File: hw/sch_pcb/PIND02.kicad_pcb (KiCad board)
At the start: 2 copper layers, 40.1 x 40.1 mm, 8 parts, among them J1 Umin ... Umax, M1 HOLE M3, M2 HOLE M3, M3 HOLE, M4 HOLE

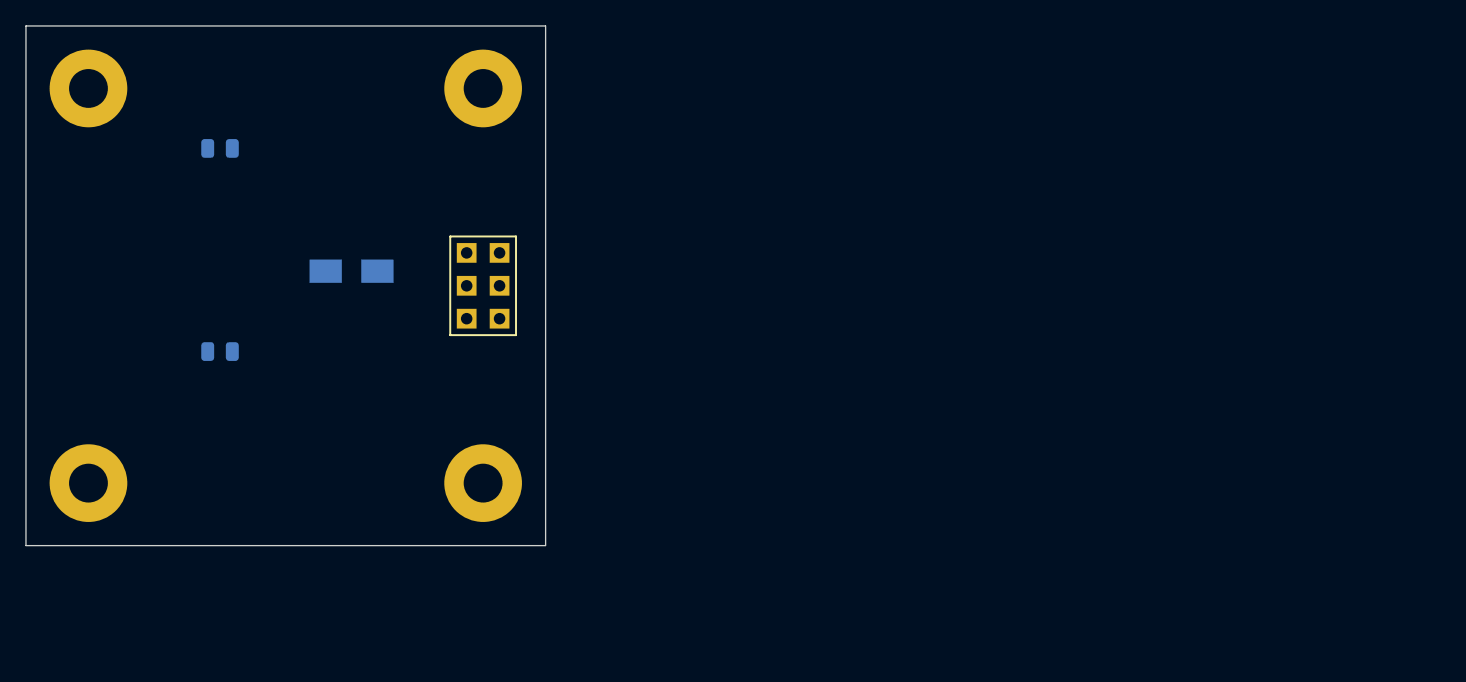
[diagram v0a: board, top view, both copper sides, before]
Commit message: Assing footprints to components. Starting of PCB design.
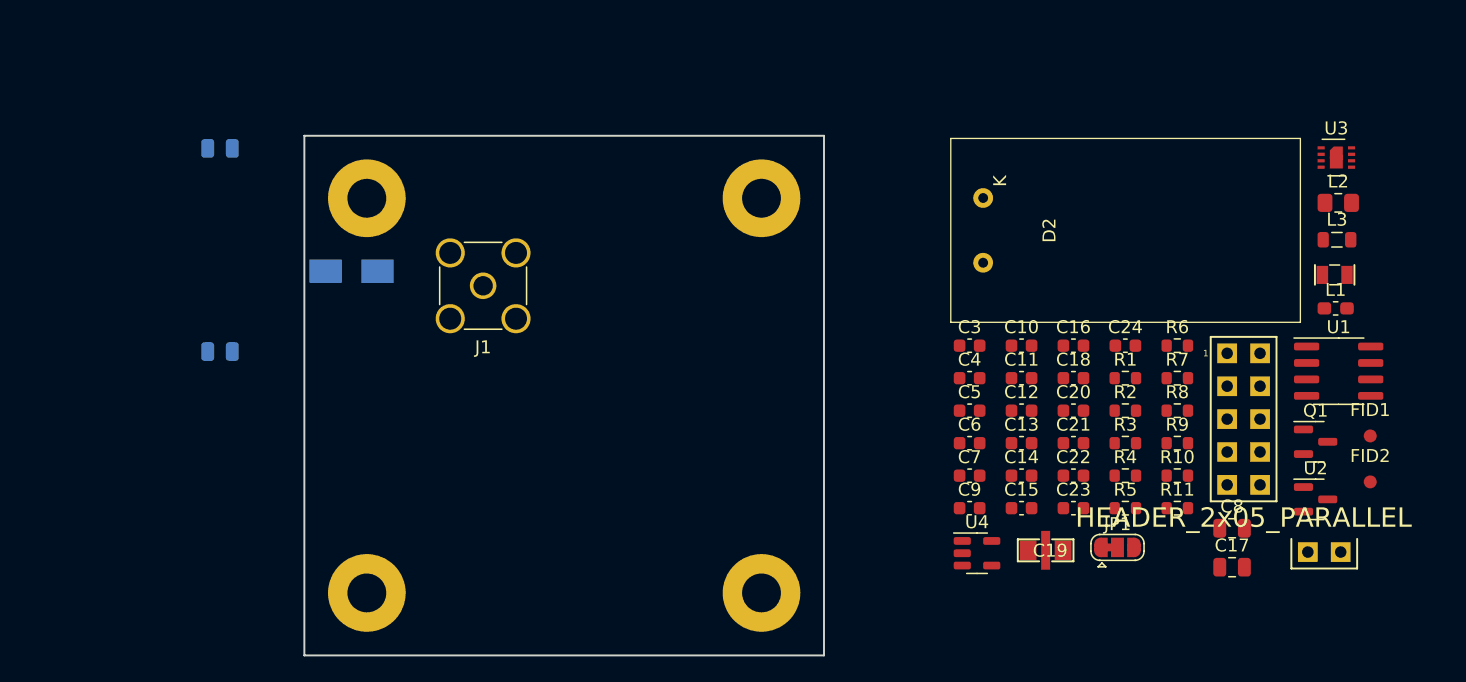
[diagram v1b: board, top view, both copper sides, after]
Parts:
- added C10: 10uF, Capacitor_SMD:C_0603_1608Metric, F.Cu at (183.8, 101.1)
- added C11: 100nF, Capacitor_SMD:C_0603_1608Metric, F.Cu at (183.8, 103.7)
- added C12: 1uF, Capacitor_SMD:C_0603_1608Metric, F.Cu at (183.8, 106.2)
- added C13: 100nF, Capacitor_SMD:C_0603_1608Metric, F.Cu at (183.8, 108.7)
- added C14: 100nF, Capacitor_SMD:C_0603_1608Metric, F.Cu at (183.8, 111.2)
- added C15: 1uF, Capacitor_SMD:C_0603_1608Metric, F.Cu at (183.8, 113.7)
- added C16: 3n3, Capacitor_SMD:C_0603_1608Metric, F.Cu at (187.8, 101.1)
- added C17: 100nF, Capacitor_SMD:C_0805_2012Metric, F.Cu at (200.1, 118.3)
- added C18: 100nF, Capacitor_SMD:C_0603_1608Metric, F.Cu at (187.8, 103.7)
- added C19: NFM21PC105-1uF, Mlab_L:FIR_0805, F.Cu at (185.7, 117.0)
- added C20: 100nF, Capacitor_SMD:C_0603_1608Metric, F.Cu at (187.8, 106.2)
- added C21: 10uF, Capacitor_SMD:C_0603_1608Metric, F.Cu at (187.8, 108.7)
- added C22: 100nF, Capacitor_SMD:C_0603_1608Metric, F.Cu at (187.8, 111.2)
- added C23: 10uF, Capacitor_SMD:C_0603_1608Metric, F.Cu at (187.8, 113.7)
- added C24: 10uF, Capacitor_SMD:C_0603_1608Metric, F.Cu at (191.8, 101.1)
- added C3: 100nF, Capacitor_SMD:C_0603_1608Metric, F.Cu at (179.8, 101.1)
- added C4: 10uF, Capacitor_SMD:C_0603_1608Metric, F.Cu at (179.8, 103.7)
- added C5: 1uF, Capacitor_SMD:C_0603_1608Metric, F.Cu at (179.8, 106.2)
- added C6: 100nF, Capacitor_SMD:C_0603_1608Metric, F.Cu at (179.8, 108.7)
- added C7: 10uF, Capacitor_SMD:C_0603_1608Metric, F.Cu at (179.8, 111.2)
- added C8: 1pF/NP0 251R15S1R0AV4E, Capacitor_SMD:C_0805_2012Metric, F.Cu at (200.1, 115.2)
- added C9: 10uF, Capacitor_SMD:C_0603_1608Metric, F.Cu at (179.8, 113.7)
- added D2: S2744-09, Mlab_D:HAMAMATSU_S2744-09, F.Cu at (191.9, 92.2)
- added FID1: Fiducial, Fiducial:Fiducial_1mm_Mask2mm, F.Cu at (210.8, 108.1)
- added FID2: Fiducial, Fiducial:Fiducial_1mm_Mask2mm, F.Cu at (210.8, 111.7)
- added J2: HEADER_2x05_PARALLEL, Mlab_Pin_Headers:Straight_2x05, F.Cu at (201.0, 106.8)
- added J3: HEADER_2x01, Mlab_Pin_Headers:Straight_2x01, F.Cu at (207.2, 117.1)
- added JP1: Address select, Jumper:SolderJumper-3_P1.3mm_Bridged12_RoundedPad1.0x1.5mm, F.Cu at (191.2, 116.7)
- added L1: NL03KT330, Inductor_SMD:L_0603_1608Metric_Pad1.05x0.95mm_HandSolder, F.Cu at (208.1, 98.3)
- added L2: DFE252012P-4R7M, Inductor_SMD:L_0805_2012Metric_Pad1.15x1.40mm_HandSolder, F.Cu at (208.3, 90.1)
- added L3: L, Inductor_SMD:L_0805_2012Metric, F.Cu at (208.2, 93.0)
- added Q1: 2SK2394-6, Package_TO_SOT_SMD:SOT-23, F.Cu at (206.5, 108.6)
- added R1: 470R, Resistor_SMD:R_0603_1608Metric, F.Cu at (191.8, 103.7)
- added R10: 4k7, Resistor_SMD:R_0603_1608Metric, F.Cu at (195.9, 111.2)
- added R11: 1k, Resistor_SMD:R_0603_1608Metric, F.Cu at (195.9, 113.7)
- added R12: 100, Mlab_R:SMD-0805, F.Cu at (208.0, 95.7)
- added R2: 470R, Resistor_SMD:R_0603_1608Metric, F.Cu at (191.8, 106.2)
- added R3: 4k7, Resistor_SMD:R_0603_1608Metric, F.Cu at (191.8, 108.7)
- added R4: 10M, Resistor_SMD:R_0603_1608Metric, F.Cu at (191.8, 111.2)
- added R5: 4k7, Resistor_SMD:R_0603_1608Metric, F.Cu at (191.8, 113.7)
- added R6: 4k7, Resistor_SMD:R_0603_1608Metric, F.Cu at (195.9, 101.1)
- added R7: 4k7, Resistor_SMD:R_0603_1608Metric, F.Cu at (195.9, 103.7)
- added R8: 4k7, Resistor_SMD:R_0603_1608Metric, F.Cu at (195.9, 106.2)
- added R9: 10k, Resistor_SMD:R_0603_1608Metric, F.Cu at (195.9, 108.7)
- added U1: OPA2314, Package_SO:SOIC-8_3.9x4.9mm_P1.27mm, F.Cu at (208.3, 103.1)
- added U2: ISL21080DIH312Z-TK, Package_TO_SOT_SMD:SOT-23, F.Cu at (206.5, 113.0)
- added U3: SHT31-DIS, Sensor_Humidity:Sensirion_DFN-8-1EP_2.5x2.5mm_P0.5mm_EP1.1x1.7mm, F.Cu at (208.1, 86.6)
- added U4: TPS613222ADBV, Package_TO_SOT_SMD:SOT-23-5, F.Cu at (180.4, 117.2)
- J1: value Umin ... Umax -> Conn_Coaxial; footprint Mlab_Pin_Headers:Straight_2x03 -> Connector_Coaxial:SMA_Amphenol_901-144_Vertical
- moved M2 52.7 mm to (163.7, 89.8)
- moved M4 23.1 mm to (163.7, 120.2)
- moved M3 23.1 mm to (133.3, 120.2)
- moved M1 12.4 mm to (133.3, 89.8)
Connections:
- C1 pad 1: +5V -> VDD
- C2 pad 1: +5V -> VDD
- D1 pad 1: +5V -> VDD
- J1 pad 1: GND -> Net-(J1-In)
